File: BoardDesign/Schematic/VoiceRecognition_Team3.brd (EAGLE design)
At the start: 92.7 x 63.5 mm, 52 parts, among them J1 5.5x2.1mm Barrel, Q1 16MHz, X1 USB-A

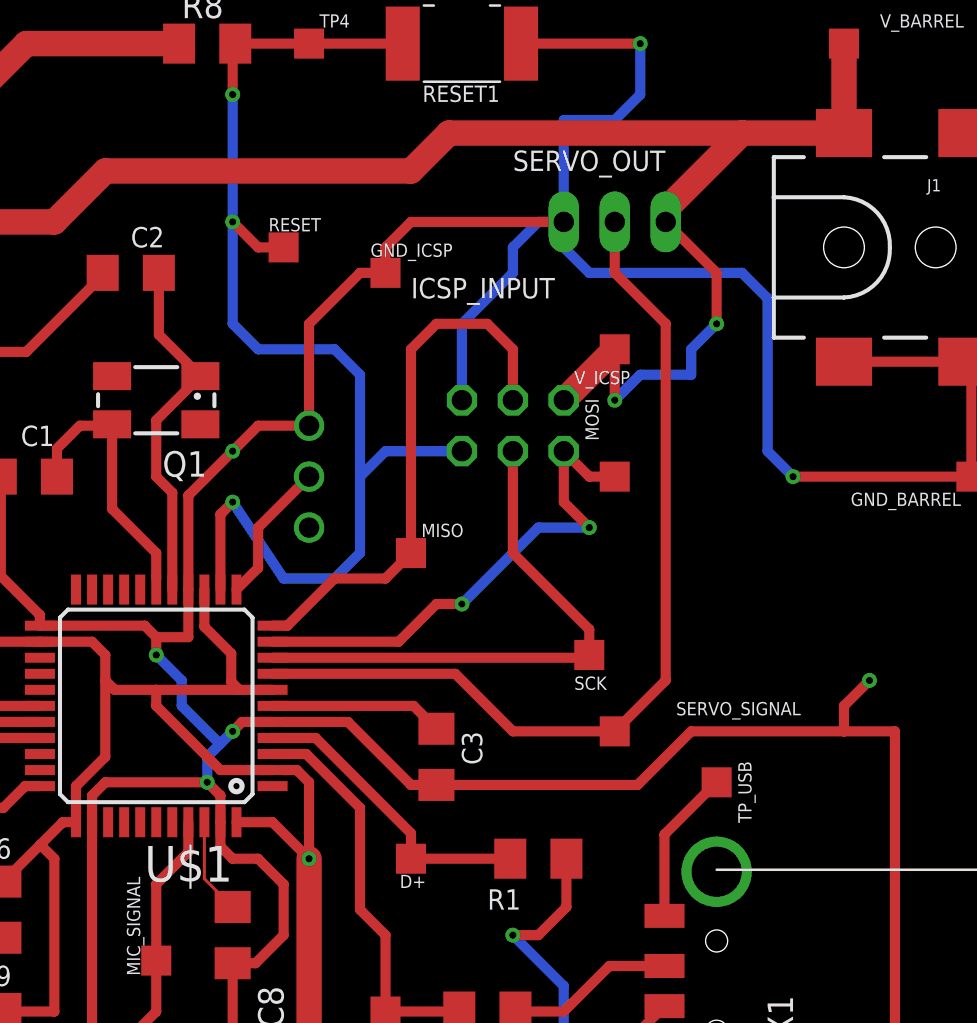
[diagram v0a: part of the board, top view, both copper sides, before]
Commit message: Rearranged a few silkscreen labels on the layout
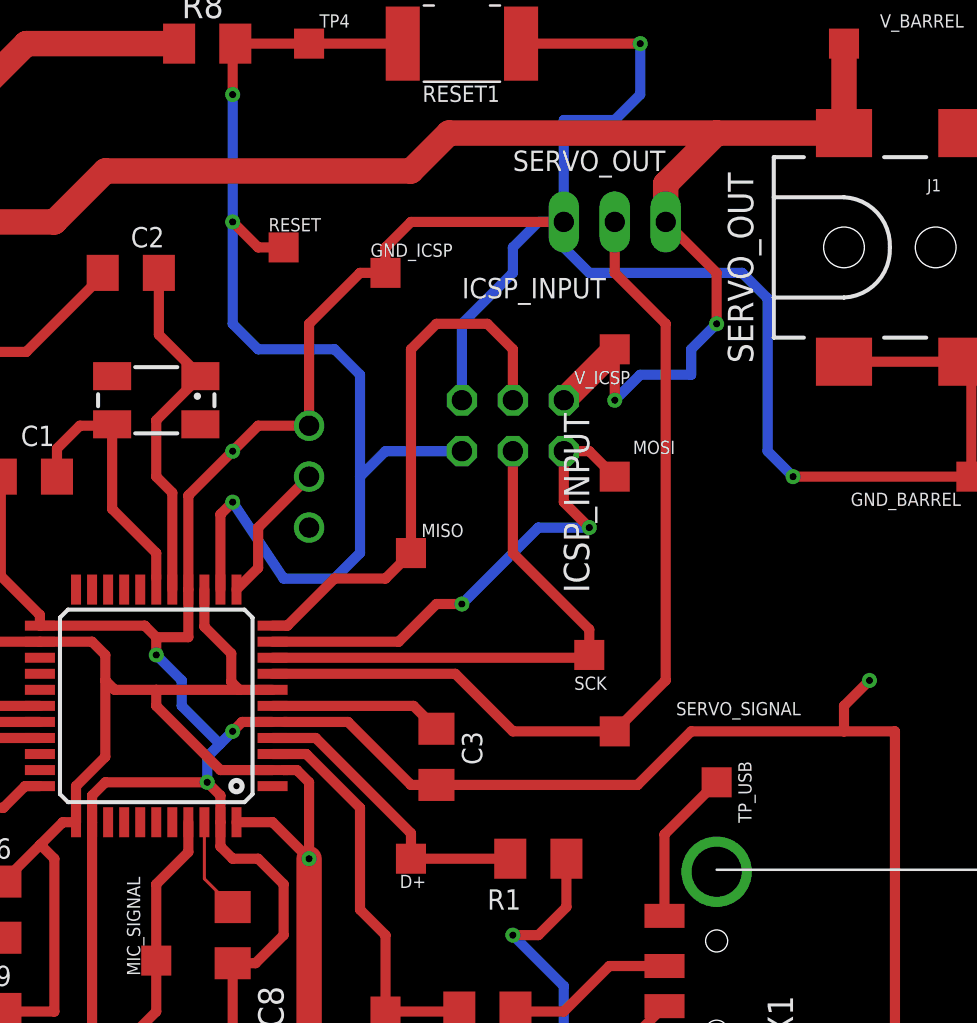
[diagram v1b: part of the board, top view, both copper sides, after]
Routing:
- net VCC: track 295.6 -> 295.1 mm

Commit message: Moved items away from edge of board.
Moved the following items:
* SERVO_OUT, RESET button
* TP GND
* VCC at bottom of board between TP VCC and MIC_INPUT
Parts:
- moved RESET1 6.48 mm to (71.1, 58.4)
- moved R8 6.35 mm to (58.4, 59.7)
- moved TP4 6.35 mm to (63.5, 59.7)
- moved MIC_INPUT 2.54 mm to (63.5, 7.62)
- moved GND_BARREL 1.27 mm to (101.6, 38.1)
- moved USB_TO_GND 1.27 mm to (94.0, 3.81)
- moved J1 1.27 mm to (95.2, 49.5)
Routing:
- net RST: track 60.9 -> 64.6 mm
- net MIC_SIGNAL: track 17.0 -> 14.4 mm
- net GND: track 400.7 -> 401.9 mm
- net VCC: track 295.1 -> 295.6 mm
